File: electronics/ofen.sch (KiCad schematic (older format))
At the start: 55 parts, among them J1 motor, J2 DC, J3 AC_IN, J4 AC_OUT, J5 AC_OUT, Q1 Q_NPN_CBE, Q2 Q_NPN_CBE, Q3 Q_NPN_CBE, Q4 Q_NPN_CBE, Q5 BTA16-600B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

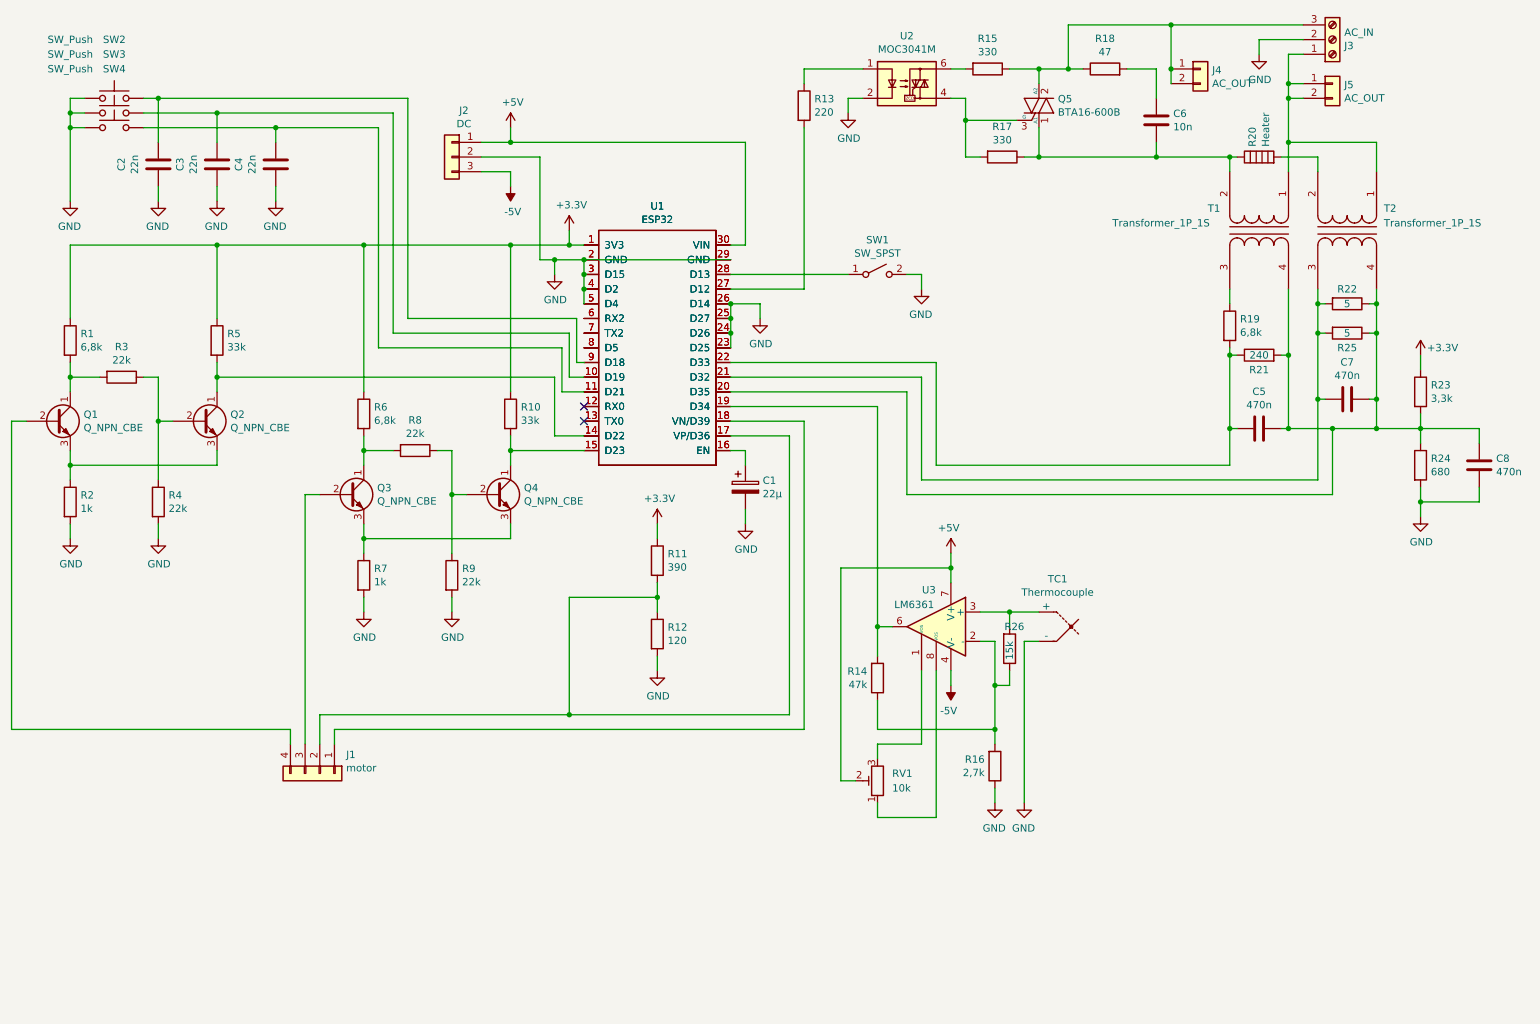
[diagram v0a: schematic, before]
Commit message: added cold junction compensation and three status leds
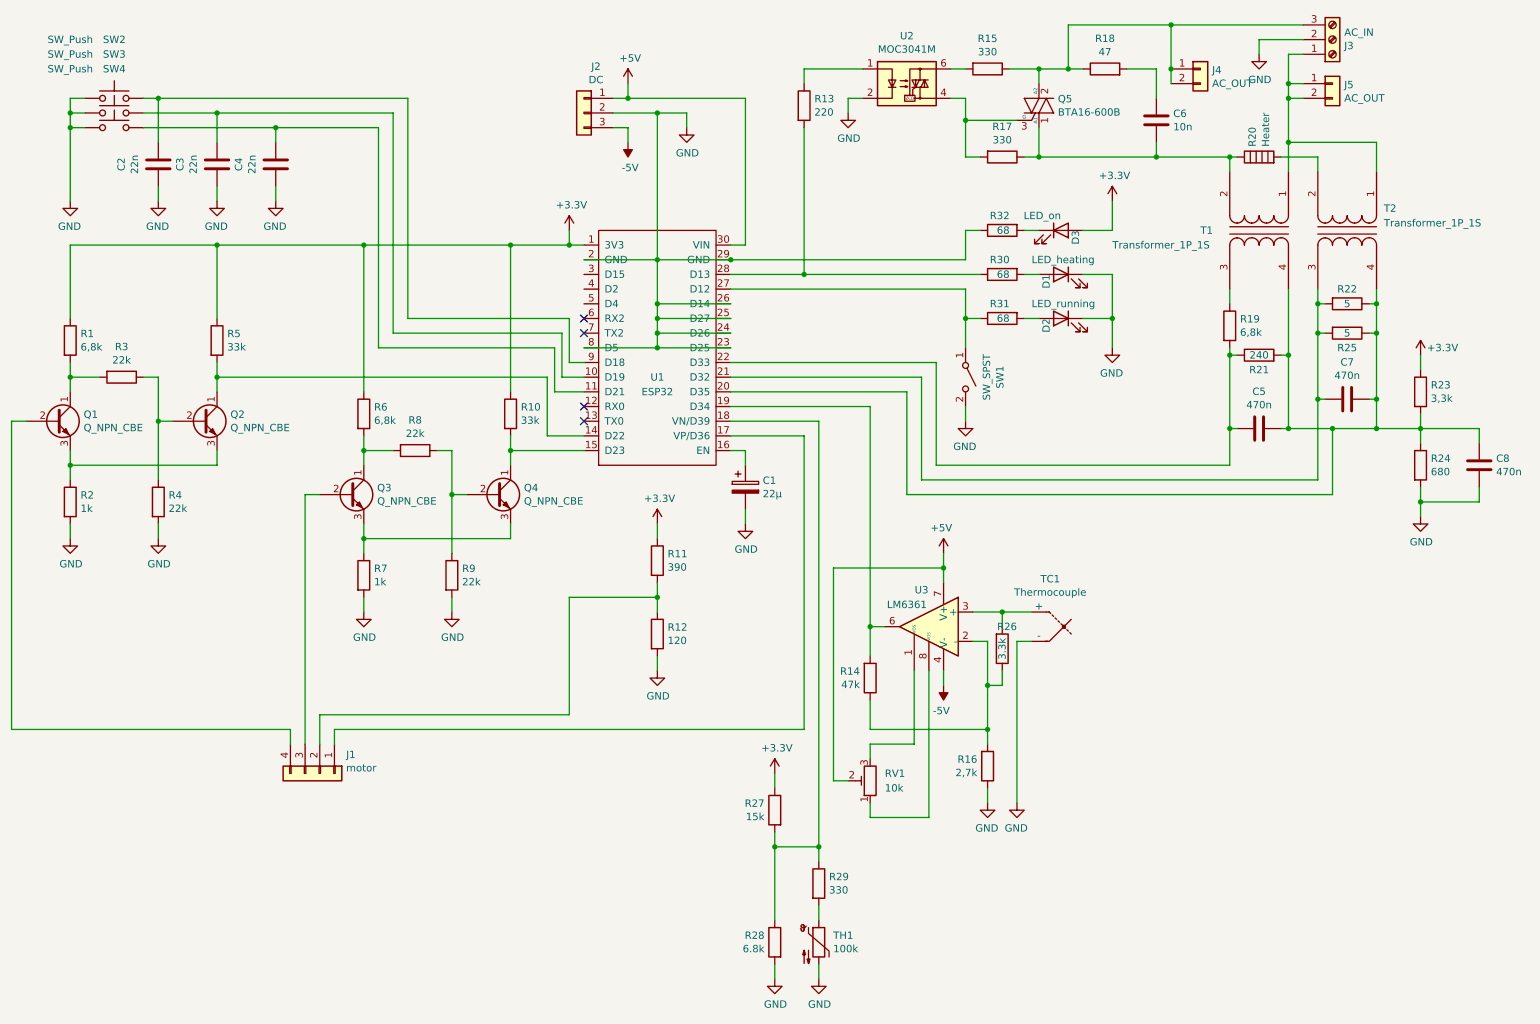
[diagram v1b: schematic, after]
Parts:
- added D1: LED_heating, Connector_PinHeader_2.54mm:PinHeader_1x02_P2.54mm_Vertical, symbol Device:LED
- added D2: LED_running, Connector_PinHeader_2.54mm:PinHeader_1x02_P2.54mm_Vertical, symbol Device:LED
- added D3: LED_on, Connector_PinHeader_2.54mm:PinHeader_1x02_P2.54mm_Vertical, symbol Device:LED
- added R27: 15k, Resistor_THT:R_Axial_DIN0207_L6.3mm_D2.5mm_P10.16mm_Horizontal, symbol Device:R
- added R28: 6.8k, Resistor_THT:R_Axial_DIN0207_L6.3mm_D2.5mm_P10.16mm_Horizontal, symbol Device:R
- added R29: 330, Resistor_THT:R_Axial_DIN0207_L6.3mm_D2.5mm_P10.16mm_Horizontal, symbol Device:R
- added R30, R31, R32: 68, Resistor_THT:R_Axial_DIN0207_L6.3mm_D2.5mm_P10.16mm_Horizontal, symbol Device:R
- added TH1: 100k, Connector_PinHeader_2.54mm:PinHeader_1x02_P2.54mm_Vertical, symbol Device:Thermistor_NTC
- C6: footprint Capacitor_THT:C_Disc_D3.8mm_W2.6mm_P2.50mm -> Capacitor_THT:C_Rect_L11.5mm_W3.5mm_P10.00mm_MKT
- R26: value 15k -> 3.3k
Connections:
- net +3V3: now also D3.2 (A), R27.1
- net GND: now also U1.8 (D5), D1.1 (K), D2.1 (K), R28.2, R32.1, TH1.2; no longer U1.3 (D15), U1.4 (D2), U1.5 (D4)
- net at J1.1 (Pin_1): now also U1.17 (VP/D36); no longer U1.18 (VN/D39)
- net at J1.2 (Pin_2), R11.2, R12.1: no longer U1.17 (VP/D36)
- net at SW1.1 (A): now also U1.27 (D12), R31.1; no longer U1.28 (D13)
- net at R13.2: now also U1.28 (D13), R30.1; no longer U1.27 (D12)
- new net: R27.2, R28.1, R29.1, U1.18 (VN/D39)
- new net: R29.2, TH1.1
- new net: D1.2 (A), R30.2
- new net: D2.2 (A), R31.2
- new net: D3.1 (K), R32.2
- no-connect marks 2 -> 4
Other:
- moved on the sheet: J2, R14, R16, R26, RV1, SW1, TC1, U3

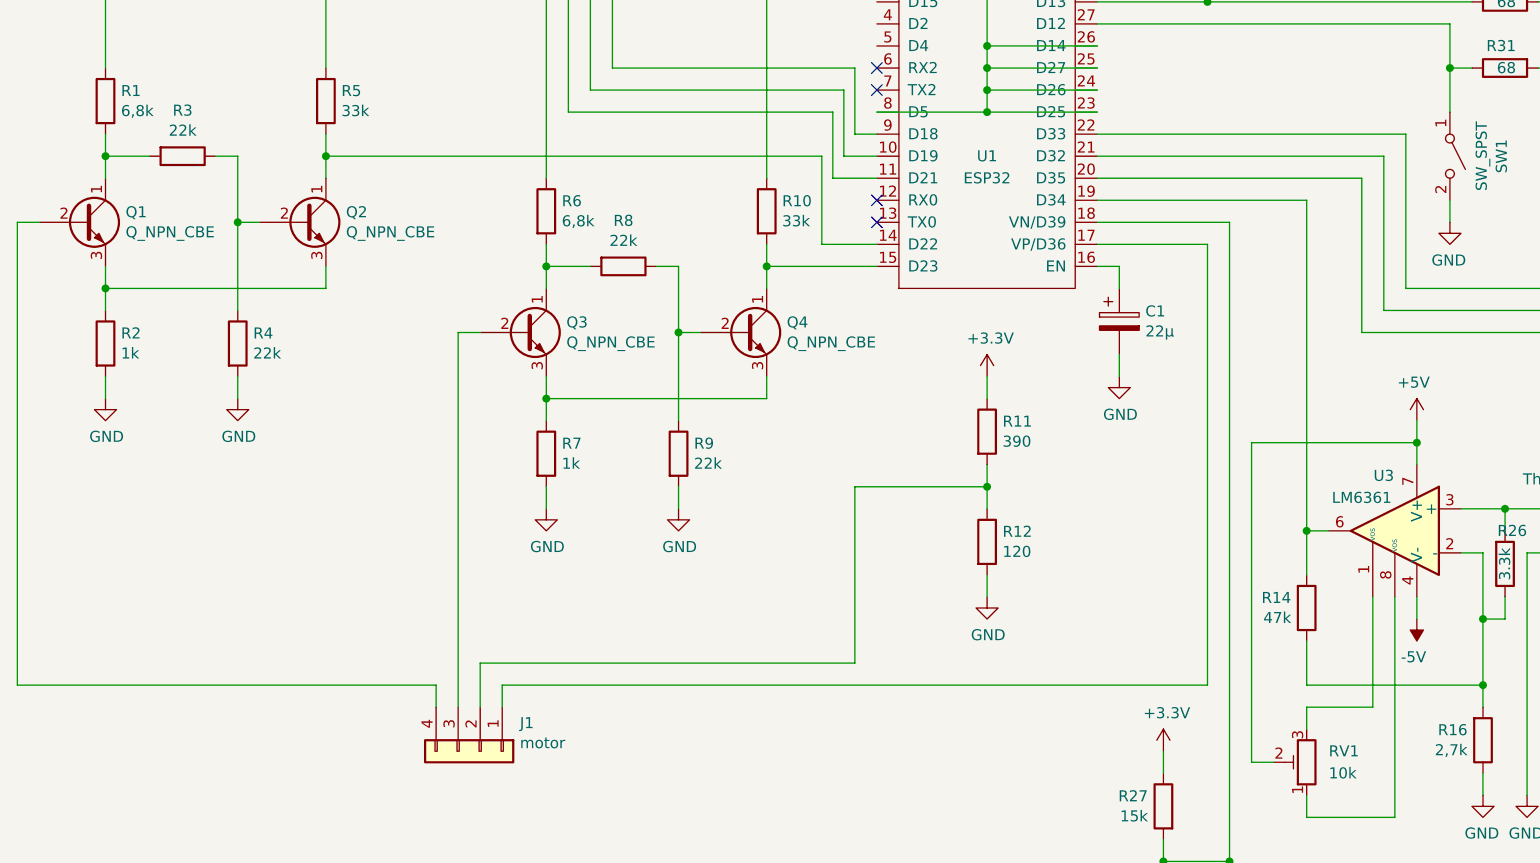
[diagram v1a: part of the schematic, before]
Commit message: redesigned PCB. smaller, better, double layer
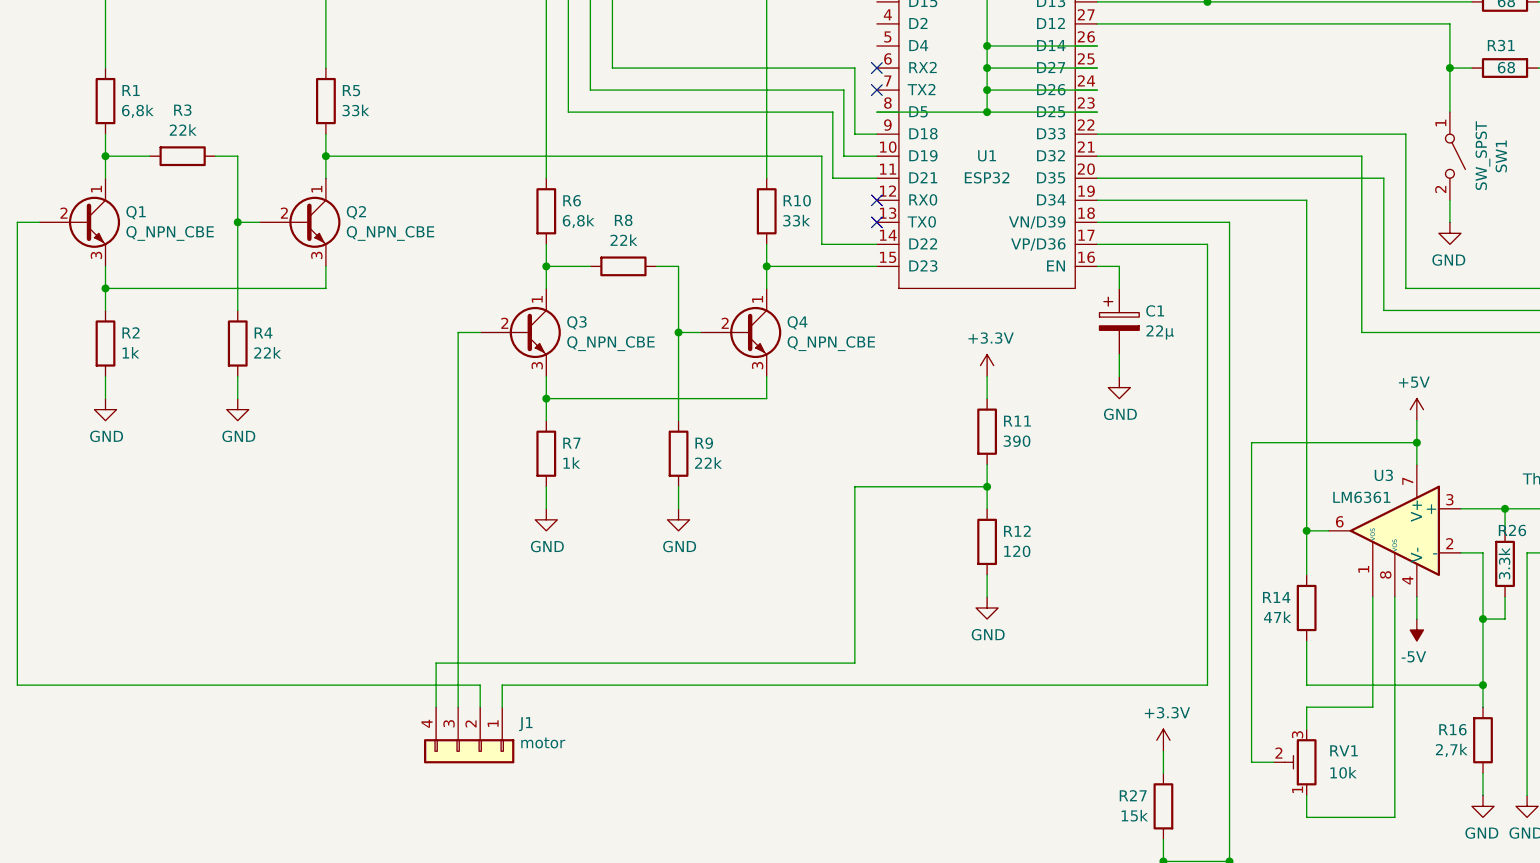
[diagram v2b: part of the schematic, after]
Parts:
- RV1: footprint Connector_PinHeader_2.54mm:PinHeader_1x03_P2.54mm_Vertical -> Potentiometer_THT:Potentiometer_Bourns_3296W_Vertical
- U2: footprint Package_DIP:DIP-6_W7.62mm_LongPads -> Package_DIP:DIP-6_W7.62mm_Socket_LongPads
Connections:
- net at C5.1, C7.1, C8.2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: now also U1.21 (D32); no longer U1.20 (D35)
- net at C7.2, R22.2, R25.2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: now also U1.20 (D35); no longer U1.21 (D32)
- net at Q1.2 (B): now also J1.2 (Pin_2); no longer J1.4 (Pin_4)
- net at R11.2, R12.1: now also J1.4 (Pin_4); no longer J1.2 (Pin_2)

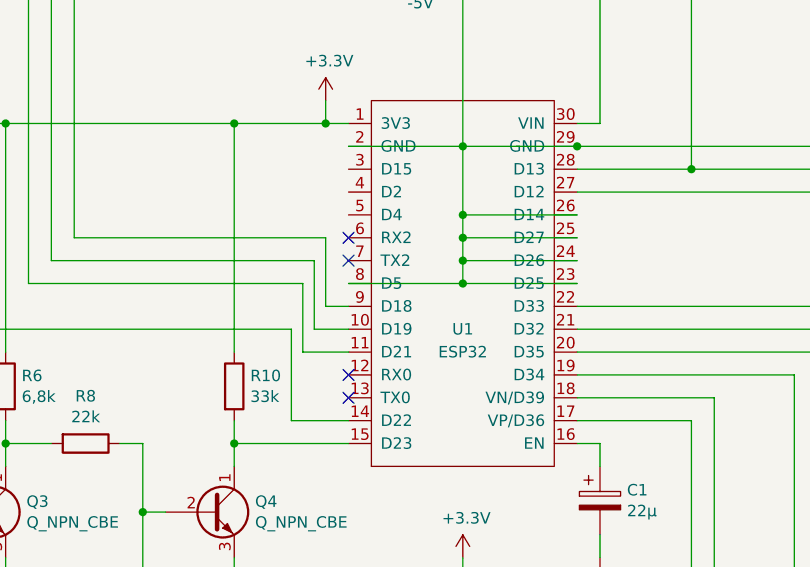
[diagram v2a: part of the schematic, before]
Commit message: removed front GND pour on PCB
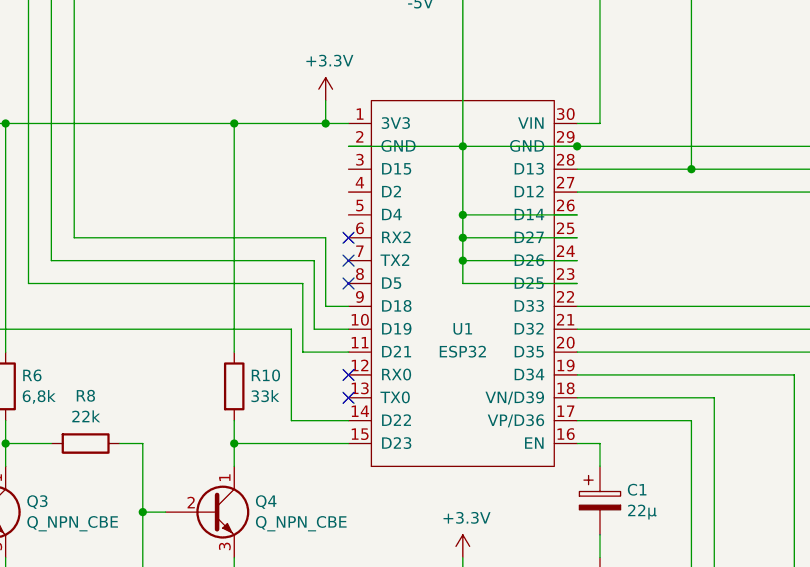
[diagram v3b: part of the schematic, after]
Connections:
- net GND: no longer U1.8 (D5)
- no-connect marks 4 -> 5
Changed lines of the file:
@@
 Connection ~ 5200 1400
 Connection ~ 5200 2400
-Wire Wire Line
-	4700 3000 5200 3000
 Connection ~ 5200 2700
 Wire Wire Line
 	5700 3000 5200 3000
-Connection ~ 5200 3000
 Wire Wire Line
 	5200 3000 5200 2900
@@
 Wire Wire Line
 	6900 3200 5700 3200
+NoConn ~ 4700 3000
 $EndSCHEMATC
